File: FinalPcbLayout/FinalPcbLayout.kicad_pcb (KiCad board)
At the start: 4 copper layers, 100.9 x 47.2 mm, 85 parts, among them J1 Conn_02x05_Odd_Even, J2 SPI, J3 Barrel_Jack, J4 C1, J5 USB_C_Receptacle, J6 Conn_01x02_Pin, J7 Display Socket, J8 Micro_SD_Card, Q1 NMOS, Q2 S8050, Q3 S8050, Q4 PMOS, Q5 PMOS, SW1 SW_Push, U1 ESP32-WROOM-E, U4 AMS1117-3.3, U7 93LCxxB, Y1 12Mhz

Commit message: Routed UART Bridge
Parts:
- added C25: 22uf, Capacitor_SMD:C_Elec_4x5.4, F.Cu at (179.3, 89.5)
- added C26: 0.1uf, Capacitor_SMD:C_0603_1608Metric, F.Cu at (176.2, 90.3)
- C5: footprint Capacitor_SMD:C_0201_0603Metric -> Capacitor_SMD:C_0603_1608Metric
- C7: footprint Capacitor_SMD:C_0603_1608Metric -> Capacitor_SMD:C_Elec_4x5.4
- J1: footprint Connector_PinHeader_1.27mm:PinHeader_2x05_P1.27mm_Vertical -> Connector_PinHeader_1.27mm:PinHeader_2x05_P1.27mm_Vertical_SMD
- moved R29 161.4 mm to (174.7, 90.3), turned to 90 degrees
- moved FB2 136.5 mm to (154.8, 112.6), turned to 90 degrees
- moved R25 115.2 mm to (140.2, 88.8), turned to 90 degrees
- moved D7 114.9 mm to (140.0, 92.2), turned to -90 degrees
- moved Q2 104.4 mm to (144.4, 119.0), turned to 90 degrees
- moved Q3 104.4 mm to (144.4, 124.5), turned to 90 degrees
- moved R22 104.1 mm to (140.1, 119.0), turned to -90 degrees
- moved R26 102.6 mm to (138.6, 119.0), turned to 90 degrees
- moved C23 102.0 mm to (134.0, 119.0), turned to -90 degrees
- moved R27 101.2 mm to (137.1, 119.0), turned to 90 degrees
- moved C24 100.5 mm to (131.0, 106.3), turned to 180 degrees
- moved R28 99.8 mm to (135.5, 119.0), turned to 90 degrees
- moved C22 99.7 mm to (130.5, 103.4), turned to 90 degrees
- moved R20 99.4 mm to (130.9, 119.0), turned to 90 degrees
- moved Y1 99.2 mm to (127.6, 103.4)
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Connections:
- net Net-(U6-OSCI) renamed /usb/OSCI
- net Net-(U6-OSCO) renamed /usb/OSCO
- net Net-(U6-REF) renamed /usb/i_ref
- net Net-(U7-DI) renamed /usb/ee_pullup
- U6 pad 42: +3.3V -> +3V3
- U6 pad 6: +3.3V -> +3V3
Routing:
- net /SCLK: track 254.6 -> 0.00 mm, vias 3 -> 0
- net +3.3V: track 232.4 -> 8.64 mm, vias 2 -> 0
- net /COPI: track 112.7 -> 0.00 mm, vias 3 -> 0
- net unconnected-(J7-Pin_9-Pad9): track 101.1 -> 0.00 mm, vias 2 -> 0
- net /Display_DC: track 101.0 -> 0.00 mm, vias 2 -> 0
- net /Display_RST: track 100.9 -> 0.00 mm, vias 2 -> 0
- net /Display_CS: track 97.3 -> 0.00 mm, vias 2 -> 0
- net +3V3: track 1.41 -> 49.0 mm, vias 1 -> 13
- net /usb/DTR: track 0.00 -> 45.6 mm, vias 0 -> 1
- net /usb/RTS: track 0.00 -> 42.5 mm, vias 0 -> 1
- net /IO22: track 28.2 -> 0.00 mm, vias 2 -> 0
- net /IO17: track 27.9 -> 0.00 mm
- net /JTAG_TDO: track 0.00 -> 26.8 mm
- net +1V2: track 0.46 -> 26.0 mm, vias 0 -> 6
- net /IO21: track 25.2 -> 0.00 mm, vias 2 -> 0
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
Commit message: Final Pcb Routed (without headers)
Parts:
- H1, H2, H3, H4: footprint MountingHole:MountingHole_3.2mm_M3 -> MountingHole:MountingHole_2.2mm_M2_Pad
- moved J3 69.0 mm to (116.6, 93.0), turned to 180 degrees
- moved Q5 63.9 mm to (116.6, 95.8), turned to 0 degrees
- moved C11 60.9 mm to (146.2, 101.9), turned to -90 degrees
- moved C10 55.3 mm to (146.2, 97.8), turned to -90 degrees
- moved U4 44.9 mm to (153.7, 99.6), turned to -90 degrees
- moved C7 7.21 mm to (93.5, 123.7)
- moved H2 3.86 mm to (87.0, 126.1)
- moved J2 3.13 mm to (167.8, 125.7)
- moved J4 3.13 mm to (158.7, 125.7)
- moved H4 2.76 mm to (179.3, 124.9)
- moved C22 2.61 mm to (130.5, 106.0)
- moved Y1 2.61 mm to (127.6, 106.0)
- moved C20 2.61 mm to (123.2, 106.0)
- moved C21 2.61 mm to (124.7, 106.0)
- moved C23 2.61 mm to (134.0, 121.6)
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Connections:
- J4 pad 1: /C1_PWM -> /C1_Limit
- J4 pad 2: /C1_CS -> /C1_PWM
- J4 pad 3: /C1_Limit -> /C1_CS
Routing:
- net /COPI: track 0.00 -> 179.2 mm, vias 0 -> 3
- net /CIPO: track 0.00 -> 161.4 mm, vias 0 -> 2
- net /SCLK: track 0.00 -> 158.3 mm, vias 0 -> 5
- net +3.3V: track 8.64 -> 163.2 mm, vias 0 -> 2
- net /Touch_CS: track 0.00 -> 103.7 mm, vias 0 -> 1
- net /Display_RST: track 0.00 -> 101.9 mm, vias 0 -> 2
- net /Display_DC: track 0.00 -> 101.8 mm, vias 0 -> 1
- net /Display_CS: track 0.00 -> 100.0 mm, vias 0 -> 1
- net /Power/V_in: track 41.3 -> 106.4 mm, vias 0 -> 2
- net /TXD: track 0.02 -> 64.9 mm, vias 1 -> 2
- net /RXD: track 0.02 -> 64.0 mm, vias 1 -> 2
- net /ESP_EN: track 7.35 -> 64.7 mm, vias 4 -> 5
- net /C1_Limit: track 0.00 -> 51.6 mm, vias 0 -> 2
- net /C1_PWM: track 0.00 -> 46.8 mm, vias 0 -> 2
- net /C1_CS: track 0.00 -> 34.1 mm
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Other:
- board size 100.9 x 47.2 mm -> 103 x 50 mm

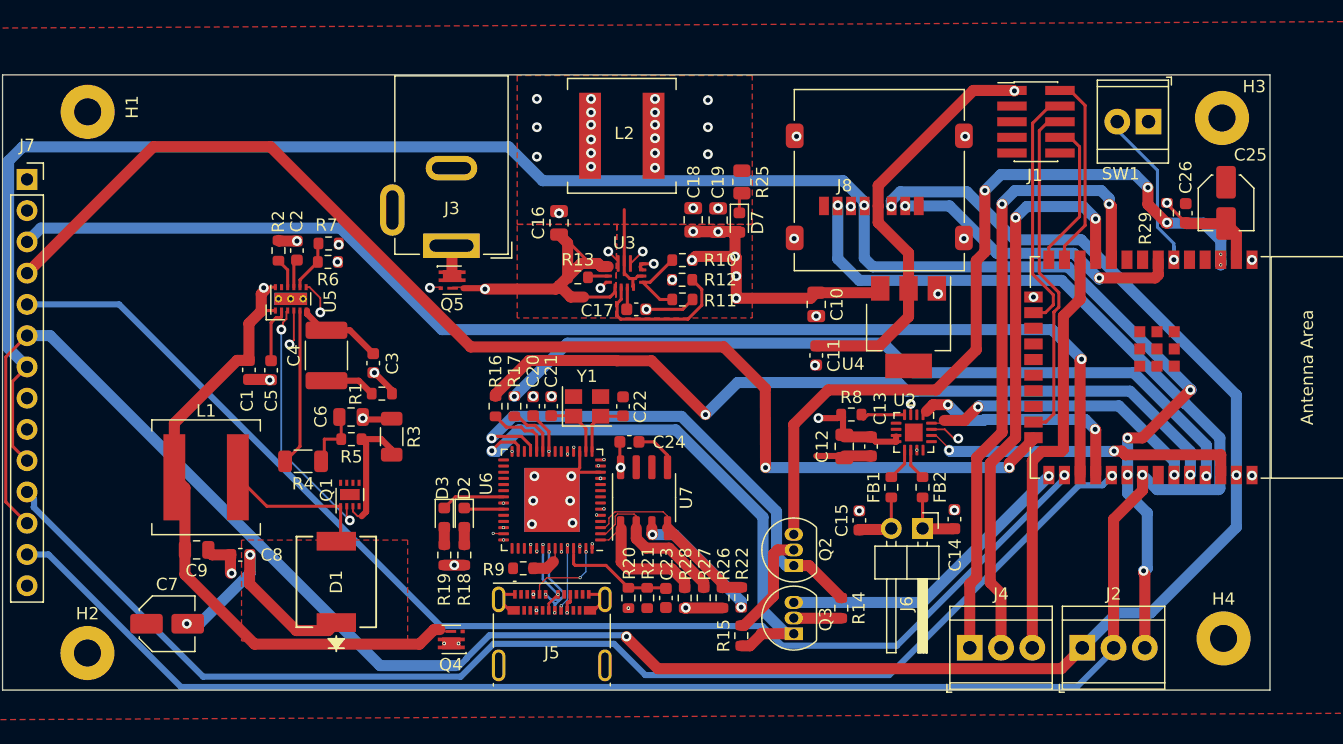
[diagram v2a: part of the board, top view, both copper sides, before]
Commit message: Added VOut Rails
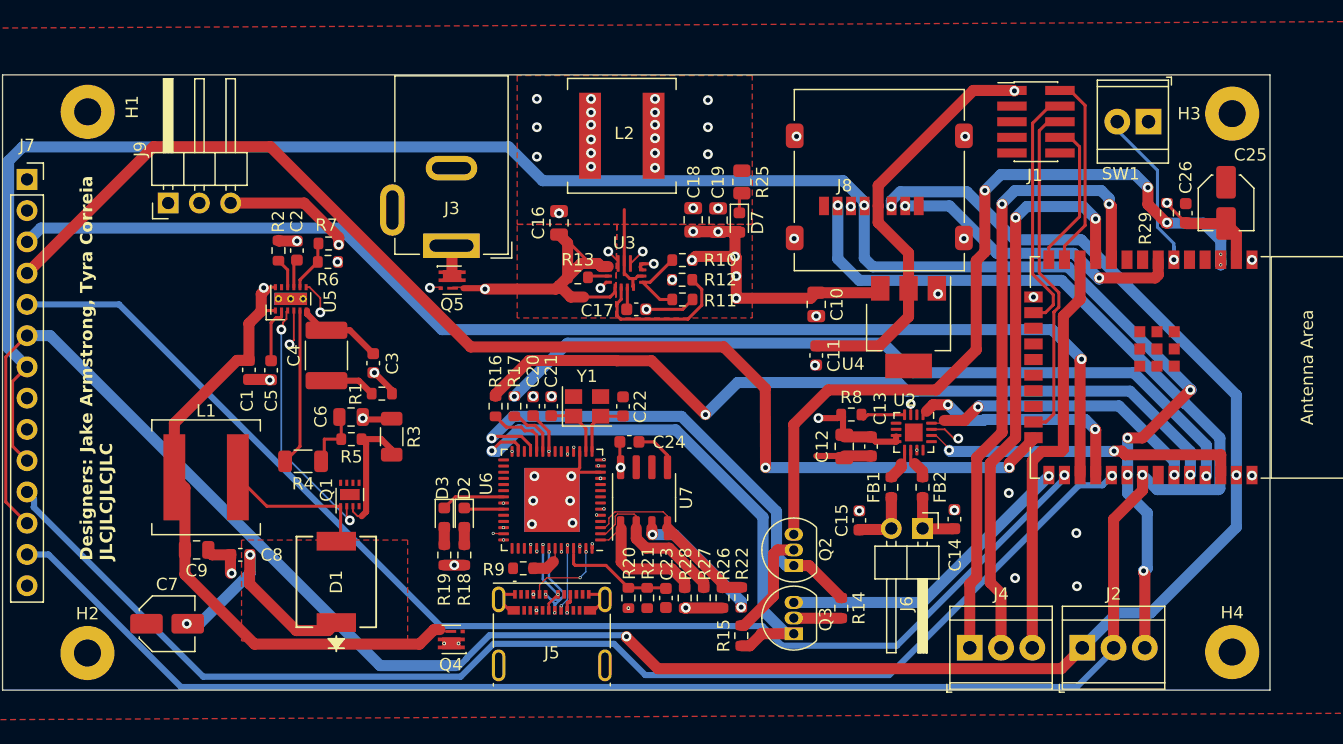
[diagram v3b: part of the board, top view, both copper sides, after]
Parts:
- added J9: Conn_01x03_Pin, Connector_PinHeader_2.54mm:PinHeader_1x03_P2.54mm_Horizontal, F.Cu at (93.5, 89.5)
- moved H4 1.31 mm to (180.0, 126.0)
- moved H3 0.90 mm to (180.0, 82.2)
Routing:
- net +12V: track 48.9 -> 59.4 mm
- net +3.3V: track 163.2 -> 166.7 mm
- net GND: vias 45 -> 49
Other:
- board text added: "+3V3 GND"
- board text added: "5-12V ->)Gnd"
- board text added: "COPI CIPO SCLK"
- board text added: "Designers: Jake Armstrong, Tyra Correia JLCJLCJLCJLC"
- board text added: "GND +3V3 +12"
- board text added: "Limit PWM CS"
- board text added: "Speaker"

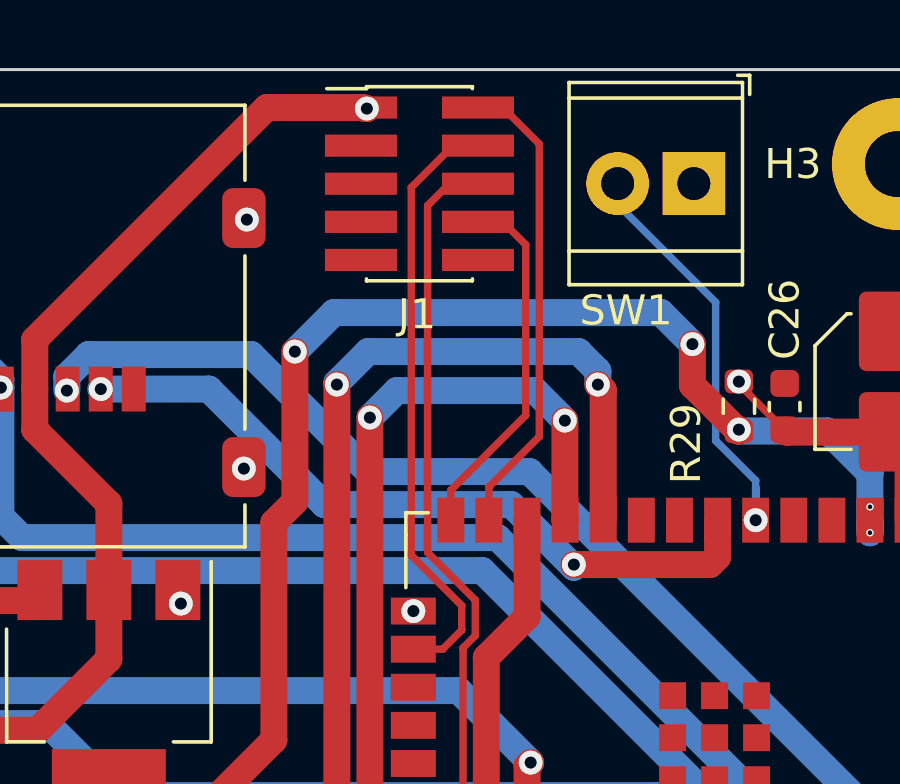
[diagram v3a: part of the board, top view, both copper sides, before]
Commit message: Added drawings.
Marginal layout changes. Does not affect board design. See tagged revision for what was sent to the board house.
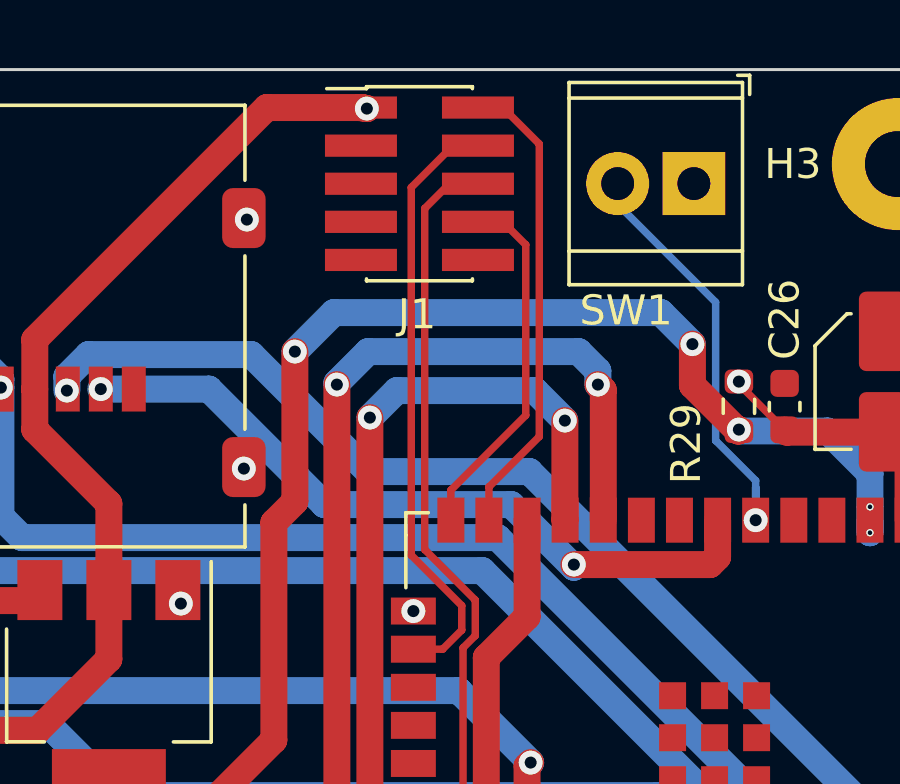
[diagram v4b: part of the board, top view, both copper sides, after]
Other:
- board text added: "M2 Screw Holes"
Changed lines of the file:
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@@
   )
   (paper "A4")
+  (title_block
+    (title "OSMI-Pump 2024 Final")
+    (date "2024-01-25")
+    (rev "3.0")
+    (company "Rose-Hulman Institute of Technology")
+    (comment 1 "Authors: Jake Armstrong, Tyra Correia")
+  )
   (layers
     (0 "F.Cu" mixed)
@@
     (effects (font (size 1 1) (thickness 0.25) bold) (justify left bottom))
   )
-  (dimension (type aligned) (layer "F.SilkS")
-    (pts (xy 82.13 79.1) (xy 183.16 78.73))
-    (height -10.642682)
-    (gr_text "101.0307 mm" (at 132.601812 67.122397 0.2098321651) (layer "F.SilkS")
+  (gr_text "M2 Screw Holes" (at 192 159) (layer "Dwgs.User")
+    (effects (font (size 5 5) (thickness 0.4)) (justify left bottom))
+  )
+  (dimension (type aligned) (layer "Dwgs.User")
+    (pts (xy 180 126) (xy 180 129.1))
+    (height -7.8)
+    (gr_text "3.1000 mm" (at 186.65 127.55 90) (layer "Dwgs.User")
+      (effects (font (size 1 1) (thickness 0.15)))
+    )
+    (format (prefix "") (suffix "") (units 3) (units_format 1) (precision 4))
+    (style (thickness 0.15) (arrow_length 1.27) (text_position_mode 0) (extension_height 0.58642) (extension_offset 0.5) keep_text_aligned)
+  )
+  (dimension (type aligned) (layer "Dwgs.User")
+    (pts (xy 183.07 79.1) (xy 80.08 79.1))
+    (height 19.1)
+    (gr_text "102.9900 mm" (at 131.575 58.85) (layer "Dwgs.User")
+      (effects (font (size 1 1) (thickness 0.15)))
+    )
+    (format (prefix "") (suffix "") (units 3) (units_format 1) (precision 4))
+    (style (thickness 0.15) (arrow_length 1.27) (text_position_mode 0) (extension_height 0.58642) (extension_offset 0.5) keep_text_aligned)
+  )
+  (dimension (type aligned) (layer "Dwgs.User")
+    (pts (xy 86.98 126.08) (xy 80.08 126.08))
+    (height -7.35)
+    (gr_text "6.9000 mm" (at 83.53 132.28) (layer "Dwgs.User")
+      (effects (font (size 1 1) (thickness 0.15)))
+    )
+    (format (prefix "") (suffix "") (units 3) (units_format 1) (precision 4))
+    (style (thickness 0.15) (arrow_length 1.27) (text_position_mode 0) (extension_height 0.58642) (extension_offset 0.5) keep_text_aligned)
+  )
+  (dimension (type aligned) (layer "Dwgs.User")
+    (pts (xy 180 82.25) (xy 183.1 82.25))
+    (height -5.648306)
+    (gr_text "3.1000 mm" (at 181.55 75.451694) (layer "Dwgs.User")
+      (effects (font (size 1 1) (thickness 0.15)))
+    )
+    (format (prefix "") (suffix "") (units 3) (units_format 1) (precision 4))
+    (style (thickness 0.15) (arrow_length 1.27) (text_position_mode 0) (extension_height 0.58642) (extension_offset 0.5) keep_text_aligned)
+  )
+  (dimension (type aligned) (layer "Dwgs.User")
+    (pts (xy 183.15 93.87) (xy 183.07 79.1))
+    (height 12.865912)
+    (gr_text "14.7702 mm" (at 197.125706 86.409085 -89.68966706) (layer "Dwgs.User")
+      (effects (font (size 1 1) (thickness 0.15)))
+    )
+    (format (prefix "") (suffix "") (units 3) (units_format 1) (precision 4))
+    (style (thickness 0.15) (arrow_length 1.27) (text_position_mode 0) (extension_height 0.58642) (extension_offset 0.5) keep_text_aligned)
+  )
+  (dimension (type aligned) (layer "Dwgs.User")
+    (pts (xy 82.07 87.59) (xy 80.1 87.6))
+    (height 10.985547)
+    (gr_text "1.9700 mm" (at 81.0234 75.45961 0.2908390224) (layer "Dwgs.User")
+      (effects (font (size 1 1) (thickness 0.15)))
+    )
+    (format (prefix "") (suffix "") (units 3) (units_format 1) (precision 4))
+    (style (thickness 0.15) (arrow_length 1.27) (text_position_mode 0) (extension_height 0.58642) (extension_offset 0.5) keep_text_aligned)
+  )
+  (dimension (type aligned) (layer "Dwgs.User")
+    (pts (xy 87 82.1) (xy 87 79.1))
+    (height -11.4)
+    (gr_text "3.0000 mm" (at 74.45 80.6 90) (layer "Dwgs.User")
+      (effects (font (size 1 1) (thickness 0.15)))
+    )
+    (format (prefix "") (suffix "") (units 3) (units_format 1) (precision 4))
+    (style (thickness 0.15) (arrow_length 1.27) (text_position_mode 0) (extension_height 0.58642) (extension_offset 0.5) keep_text_aligned)
+  )
+  (dimension (type aligned) (layer "Dwgs.User")
+    (pts (xy 189.1 93.87) (xy 189.1 111.87))
+    (height -8.15)
+    (gr_text "18.0000 mm" (at 196.1 102.87 90) (layer "Dwgs.User")
+      (effects (font (size 1 1) (thickness 0.15)))
+    )
+    (format (prefix "") (suffix "") (units 3) (units_format 1) (precision 4))
+    (style (thickness 0.15) (arrow_length 1.27) (text_position_mode 0) (extension_height 0.58642) (extension_offset 0.5) keep_text_aligned)
+  )
+  (dimension (type aligned) (layer "Dwgs.User")
+    (pts (xy 180 126) (xy 183 126))
+    (height 9.2)
+    (gr_text "3.0000 mm" (at 181.5 134.05) (layer "Dwgs.User")
+      (effects (font (size 1 1) (thickness 0.15)))
+    )
+    (format (prefix "") (suffix "") (units 3) (units_format 1) (precision 4))
+    (style (thickness 0.15) (arrow_length 1.27) (text_position_mode 0) (extension_height 0.58642) (extension_offset 0.5) keep_text_aligned)
+  )
+  (dimension (type aligned) (layer "Dwgs.User")
+    (pts (xy 189.1 93.87) (xy 183.15 93.87))
+    (height 27.12)
+    (gr_text "5.9500 mm" (at 186.125 65.6) (layer "Dwgs.User")
+      (effects (font (size 1 1) (thickness 0.15)))
+    )
+    (format (prefix "") (suffix "") (units 3) (units_format 1) (precision 4))
+    (style (thickness 0.15) (arrow_length 1.27) (text_position_mode 0) (extension_height 0.58642) (extension_offset 0.5) keep_text_aligned)
+  )
+  (dimension (type aligned) (layer "Dwgs.User")
+    (pts (xy 180 82.25) (xy 180 79.1))
+    (height 7.9)
+    (gr_text "3.1500 mm" (at 186.75 80.675 90) (layer "Dwgs.User")
+      (effects (font (size 1 1) (thickness 0.15)))
+    )
+    (format (prefix "") (suffix "") (units 3) (units_format 1) (precision 4))
+    (style (thickness 0.15) (arrow_length 1.27) (text_position_mode 0) (extension_height 0.58642) (extension_offset 0.5) keep_text_aligned)
+  )
+  (dimension (type aligned) (layer "Dwgs.User")
+    (pts (xy 87 82.1) (xy 80.1 82.1))
+    (height 9.1)
+    (gr_text "6.9000 mm" (at 83.55 71.85) (layer "Dwgs.User")
+      (effects (font (size 1 1) (thickness 0.15)))
+    )
+    (format (prefix "") (suffix "") (units 3) (units_format 1) (precision 4))
+    (style (thickness 0.15) (arrow_length 1.27) (text_position_mode 0) (extension_height 0.58642) (extension_offset 0.5) keep_text_aligned)
+  )
+  (dimension (type aligned) (layer "Dwgs.User")
+    (pts (xy 86.98 126.08) (xy 86.98 129.08))
+    (height 9.61)
+    (gr_text "3.0000 mm" (at 76.22 127.58 90) (layer "Dwgs.User")
+      (effects (font (size 1 1) (thickness 0.15)))
+    )
+    (format (prefix "") (suffix "") (units 3) (units_format 1) (precision 4))
+    (style (thickness 0.15) (arrow_length 1.27) (text_position_mode 0) (extension_height 0.58642) (extension_offset 0.5) keep_text_aligned)
+  )
+  (dimension (type aligned) (layer "Dwgs.User")
+    (pts (xy 80.08 129.09) (xy 80.08 79.1))
+    (height -11.33)
+    (gr_text "49.9900 mm" (at 67.6 104.095 90) (layer "Dwgs.User")
       (effects (font (size 1 1) (thickness 0.15)))
     )
@@
   (segment (start 165.4628 97.7828) (end 164.8256 98.42) (width 0.25) (layer "F.Cu") (net 18))
   (segment (start 163.7792 83.0292) (end 163.7792 95.285596) (width 0.25) (layer "F.Cu") (net 18))
+  (segment (start 164.2292 83.7292) (end 165.0528 82.9056) (width 0.25) (layer "F.Cu") (net 19))
+  (segment (start 164.2292 95.0992) (end 164.2292 83.7292) (width 0.25) (layer "F.Cu") (net 19))
   (segment (start 165.5064 98.375596) (end 165.9128 97.969196) (width 0.25) (layer "F.Cu") (net 19))
-  (segment (start 163.85 107.31) (end 164.85 107.31) (width 0.25) (layer "F.Cu") (net 19))
+  (segment (start 165.9128 96.7828) (end 164.2292 95.0992) (width 0.25) (layer "F.Cu") (net 19))
   (segment (start 165.9128 97.969196) (end 165.9128 96.7828) (width 0.25) (layer "F.Cu") (net 19))
-  (segment (start 165.5064 106.6536) (end 165.5064 98.375596) (width 0.25) (layer "F.Cu") (net 19))
-  (segment (start 164.325 95.195) (end 164.325 83.6334) (width 0.25) (layer "F.Cu") (net 19))
-  (segment (start 164.325 83.6334) (end 165.0528 82.9056) (width 0.25) (layer "F.Cu") (net 19))
   (segment (start 164.85 107.31) (end 165.5064 106.6536) (width 0.25) (layer "F.Cu") (net 19))
-  (segment (start 165.9128 96.7828) (end 164.325 95.195) (width 0.25) (layer "F.Cu") (net 19))
+  (segment (start 165.5064 106.6536) (end 165.5064 98.375596) (width 0.25) (layer "F.Cu") (net 19))
+  (segment (start 163.85 107.31) (end 164.85 107.31) (width 0.25) (layer "F.Cu") (net 19))
   (segment (start 167.5964 84.9392) (end 166.8328 84.1756) (width 0.25) (layer "F.Cu") (net 20))
   (segment (start 167.5964 90.6236) (end 167.5964 84.9392) (width 0.25) (layer "F.Cu") (net 20))

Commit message: Updated CSV
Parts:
- C24: value .1u -> 0.1uF
- C25: value 22uf -> 22uF
- C26: value 0.1uf -> 0.1uF
- FB1, FB2: value FerriteBead -> 120 ohm
- J1: value Conn_02x05_Odd_Even -> JTAG
- J2: value SPI -> 3Term
- J4: value C1 -> 3Term
- J6: value Conn_01x02_Pin -> Speaker_Out
- J9: value Conn_01x03_Pin -> Power Out
- L1: footprint Inductor_SMD:L_Coilcraft_XAL8050-223 -> Inductor_SMD:L_Coilcraft_XAL8080-XXX
- L2: value L -> 2.2uH; footprint Inductor_SMD:L_Coilcraft_XAL8050-223 -> Inductor_SMD:L_Coilcraft_XAL8080-XXX
- R13, R26, R27, R28, R29: value 10k -> 10k 1%
- R19: value 65 -> 68
- R5: footprint Resistor_SMD:R_0603_1608Metric -> Resistor_SMD:R_0805_2012Metric
- R7: value 27.4 -> 27.4k
- U2: value ~ -> MAX98357
- U3: value ~ -> TPS63070RNMR
- U4: value AMS1117-3.3 -> LDI1117-3.3H
- U5: value ~ -> LM51551DSSR
- U6: value ~ -> FT232HPQ
- moved L2 0.17 mm to (130.3, 83.9)
- turned C25 to 90 degrees
- turned C7 to 180 degrees
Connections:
- C25 pad 1: GND -> +3.3V
- C25 pad 2: +3.3V -> GND
- C7 pad 1: GND -> +12V
- C7 pad 2: +12V -> GND
